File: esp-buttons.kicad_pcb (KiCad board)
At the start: 2 copper layers, 81.3 x 106.9 mm, 45 parts, among them CON1 POWER_5V, P1 CONN_BUTTON1, P2 CONN_BUTTON2, P3 CONN_BUTTON3, P4 CONN_BUTTON4, P5 CONN_BUTTON5, P6 UART_DEBUG, P7 UART, P8 POWER_5V, P9 USB, Q1 IRLML2502TRPBF, Q2 IRLML2502TRPBF, Q3 IRLML2502TRPBF, Q4 IRLML2502TRPBF, Q5 IRLML2502TRPBF, SW1 RESET_BUTTON, SW2 PROG_BUTTON, U1 ESP-07v2, U2 LD1117S33CTR, U3 FT230XS

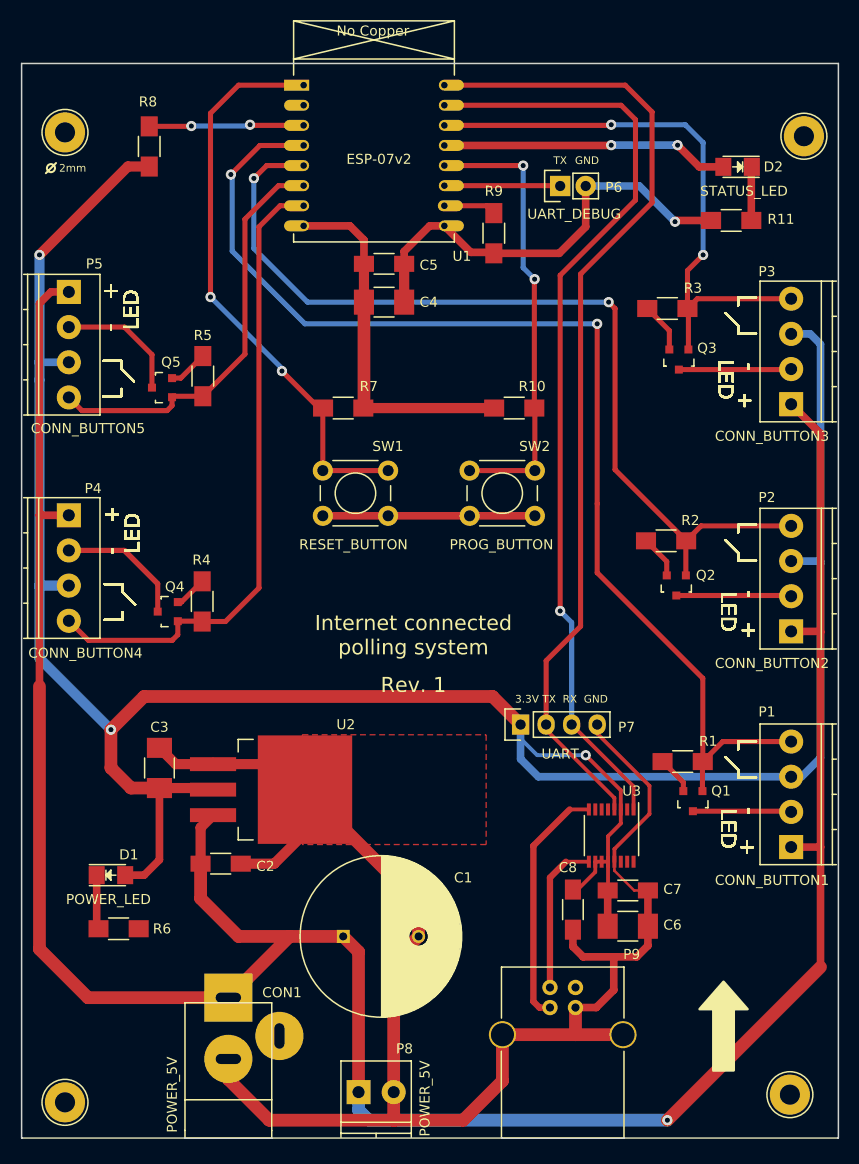
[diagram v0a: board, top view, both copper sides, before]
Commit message: Track layout - part4. Fixing some footprint's pads. Modifying the placment of the mounting holes. Added via stitches to the voltage regulator (U2)
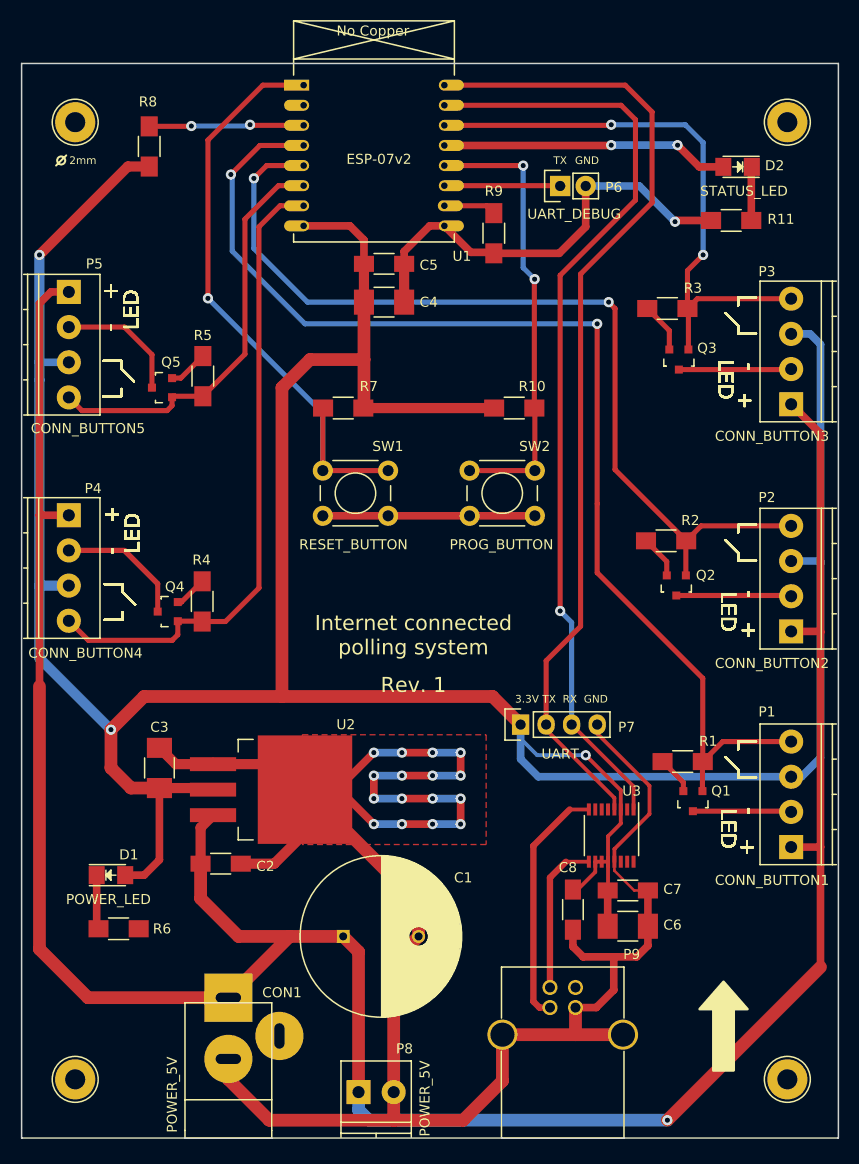
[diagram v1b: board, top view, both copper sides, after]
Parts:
- moved MT1 2.50 mm to (85.1, 168.4)
- moved MT3 2.16 mm to (156.0, 73.2)
- moved MT2 1.55 mm to (156.0, 168.4)
- moved MT4 1.44 mm to (85.1, 73.2)
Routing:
- net GND: track 251.2 -> 309.5 mm, vias 1 -> 17
- net +3V3: track 291.9 -> 331.9 mm
- net /RESET: track 57.4 -> 62.2 mm, vias 2 -> 1

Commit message: Final layout. Added bottom GND pour. Added dimentions on 'Dwgs' layer.
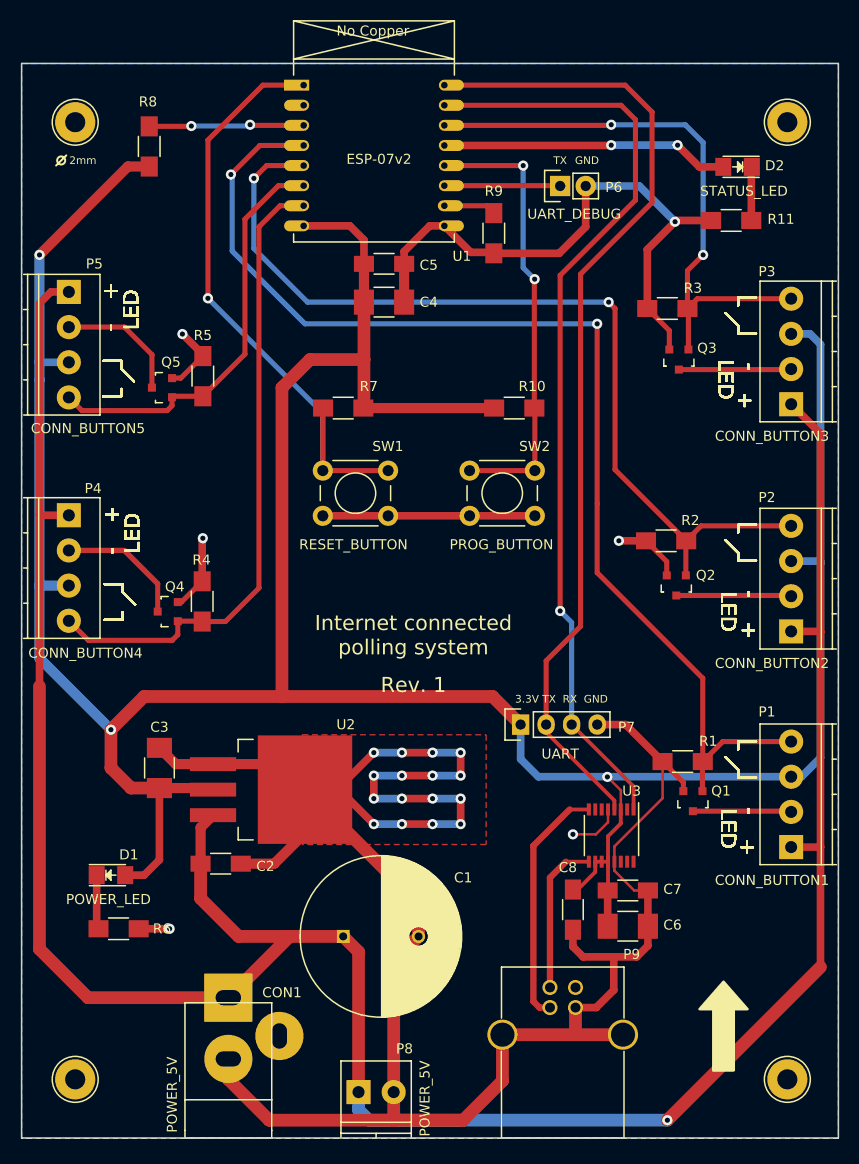
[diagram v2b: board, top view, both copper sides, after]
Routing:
- net GND: track 309.5 -> 340.4 mm, vias 17 -> 22
- net +3V3: track 331.9 -> 320.4 mm
- added copper zone on B.Cu, net GND
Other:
- net class Default: clearance 0.254 -> 0.2286
- net class POWER: clearance 0.254 -> 0.2286
- rule trace_clearance: 0.254 -> 0.2286
